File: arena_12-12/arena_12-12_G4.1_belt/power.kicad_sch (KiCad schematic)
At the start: 1 part, among them J4 Barrel_Jack

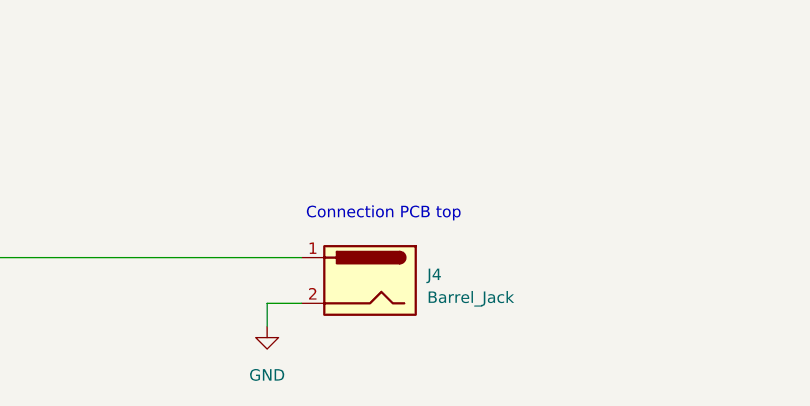
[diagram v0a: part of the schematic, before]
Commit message: cleanup, belt with SMD power connector
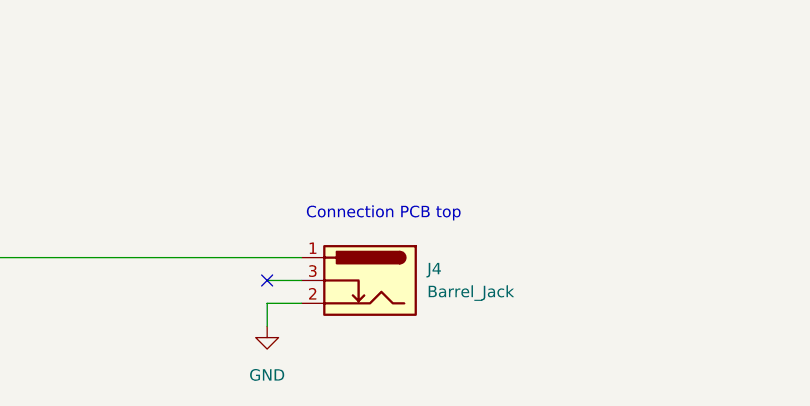
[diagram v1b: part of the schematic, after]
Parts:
- J4: footprint arena_custom:DCJACK_2PIN_HIGHCURRENT -> Connector_BarrelJack:BarrelJack_CUI_PJ-036AH-SMT_Horizontal; symbol Connector:Barrel_Jack -> Connector:Barrel_Jack_Switch; DigiKey PN CP-063AH-ND -> CP-036AHPJTR-ND; LCSC Part # C2928097 -> C3094052; MPN PJ-063AH -> PJ-036AH-SMT-TR
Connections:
- no-connect marks 0 -> 1
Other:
- title: 12-12 Teensy G4.1 Arena Belt Modular LED Display -> Arena 12-12 G4.1 Belt :: Modular LED Display
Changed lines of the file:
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@@
 	(paper "USLetter")
 	(title_block
-		(title "12-12 Teensy G4.1 Arena Belt Modular LED Display")
-		(date "2025-07-22")
-		(rev "v0.5.1")
+		(title "Arena 12-12 G4.1 Belt :: Modular LED Display")
+		(date "2025-07-24")
+		(rev "v0.1")
 		(company "MCN-NET @ Janelia")
 	)
@@
 		(effects
 			(font
+				(face "KiCad Font")
 				(size 5.08 5.08)
 				(thickness 0.508)
@@
 		)
 	)
+	(no_connect
+		(at 92.71 82.55)
+	)
 	(wire
 		(pts
@@
 		(pts
 			(xy 96.52 85.09) (xy 92.71 85.09)
+		)
+		(stroke
+			(width 0)
+			(type default)
+		)
+	)
+	(wire
+		(pts
+			(xy 92.71 82.55) (xy 96.52 82.55)
 		)
 		(stroke
@@
 	)
 	(symbol
-		(lib_id "Connector:Barrel_Jack")
+		(lib_id "Connector:Barrel_Jack_Switch")
 		(at 104.14 82.55 0)
 		(mirror y)
@@
 		(fields_autoplaced yes)
 		(property "Reference" "J4"
-			(at 110.49 81.915 0)
+			(at 110.49 81.2799 0)
 			(effects
 				(font
@@
 		)
 		(property "Value" "Barrel_Jack"
-			(at 110.49 84.455 0)
+			(at 110.49 83.8199 0)
 			(effects
 				(font
@@
 			)
 		)
-		(property "Footprint" "arena_custom:DCJACK_2PIN_HIGHCURRENT"
+		(property "Footprint" "Connector_BarrelJack:BarrelJack_CUI_PJ-036AH-SMT_Horizontal"
 			(at 102.87 83.566 0)
 			(effects
@@
 			)
 		)
-		(property "Datasheet" "https://octopart.com/datasheet/pj-063ah-same+sky-106234056"
+		(property "Datasheet" "~"
 			(at 102.87 83.566 0)
 			(effects
@@
 			)
 		)
-		(property "Description" ""
+		(property "Description" "DC Barrel Jack with an internal switch"
 			(at 104.14 82.55 0)
 			(effects
@@
 			)
 		)
-		(property "DigiKey PN" "CP-063AH-ND"
+		(property "DigiKey PN" "CP-036AHPJTR-ND"
 			(at 104.14 82.55 0)
 			(effects
@@
 			)
 		)
-		(property "LCSC Part #" "C2928097"
+		(property "LCSC Part #" "C3094052"
 			(at 104.14 82.55 0)
 			(effects
@@
 			)
 		)
-		(property "MPN" "PJ-063AH"
+		(property "MPN" "PJ-036AH-SMT-TR"
 			(at 104.14 82.55 0)
 			(effects
@@
 		(pin "2"
 		)
-		(instances
+		(pin "3"
+		)
+		(instances
